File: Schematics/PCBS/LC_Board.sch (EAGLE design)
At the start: 24 parts, among them IC1 ATMEGA328P-AU, Q10 220mA/50V/3.5Ω, U1 LT1763CS8-3.3#TRPBF

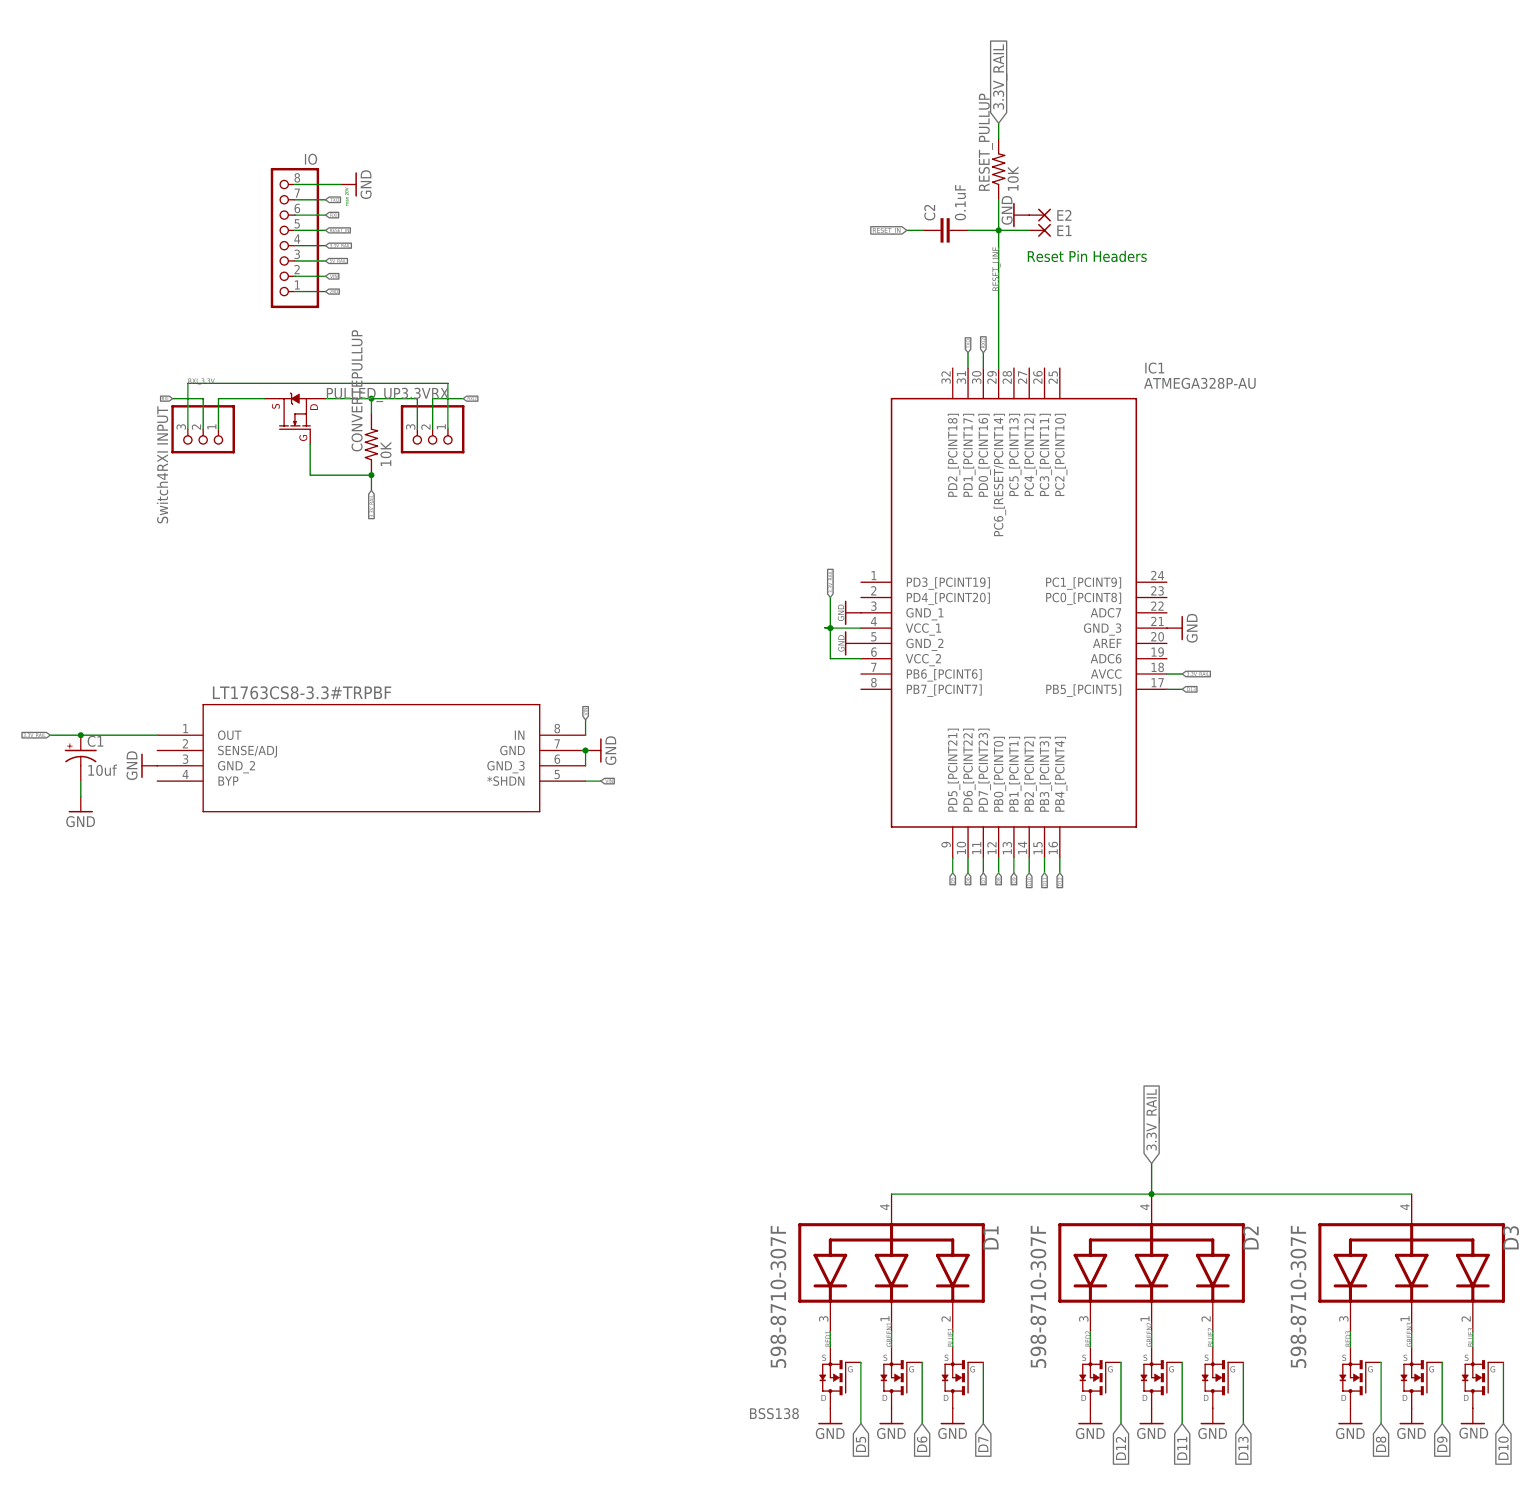
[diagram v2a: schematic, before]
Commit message: updated LC_Board IO to match need pins for Shift registers
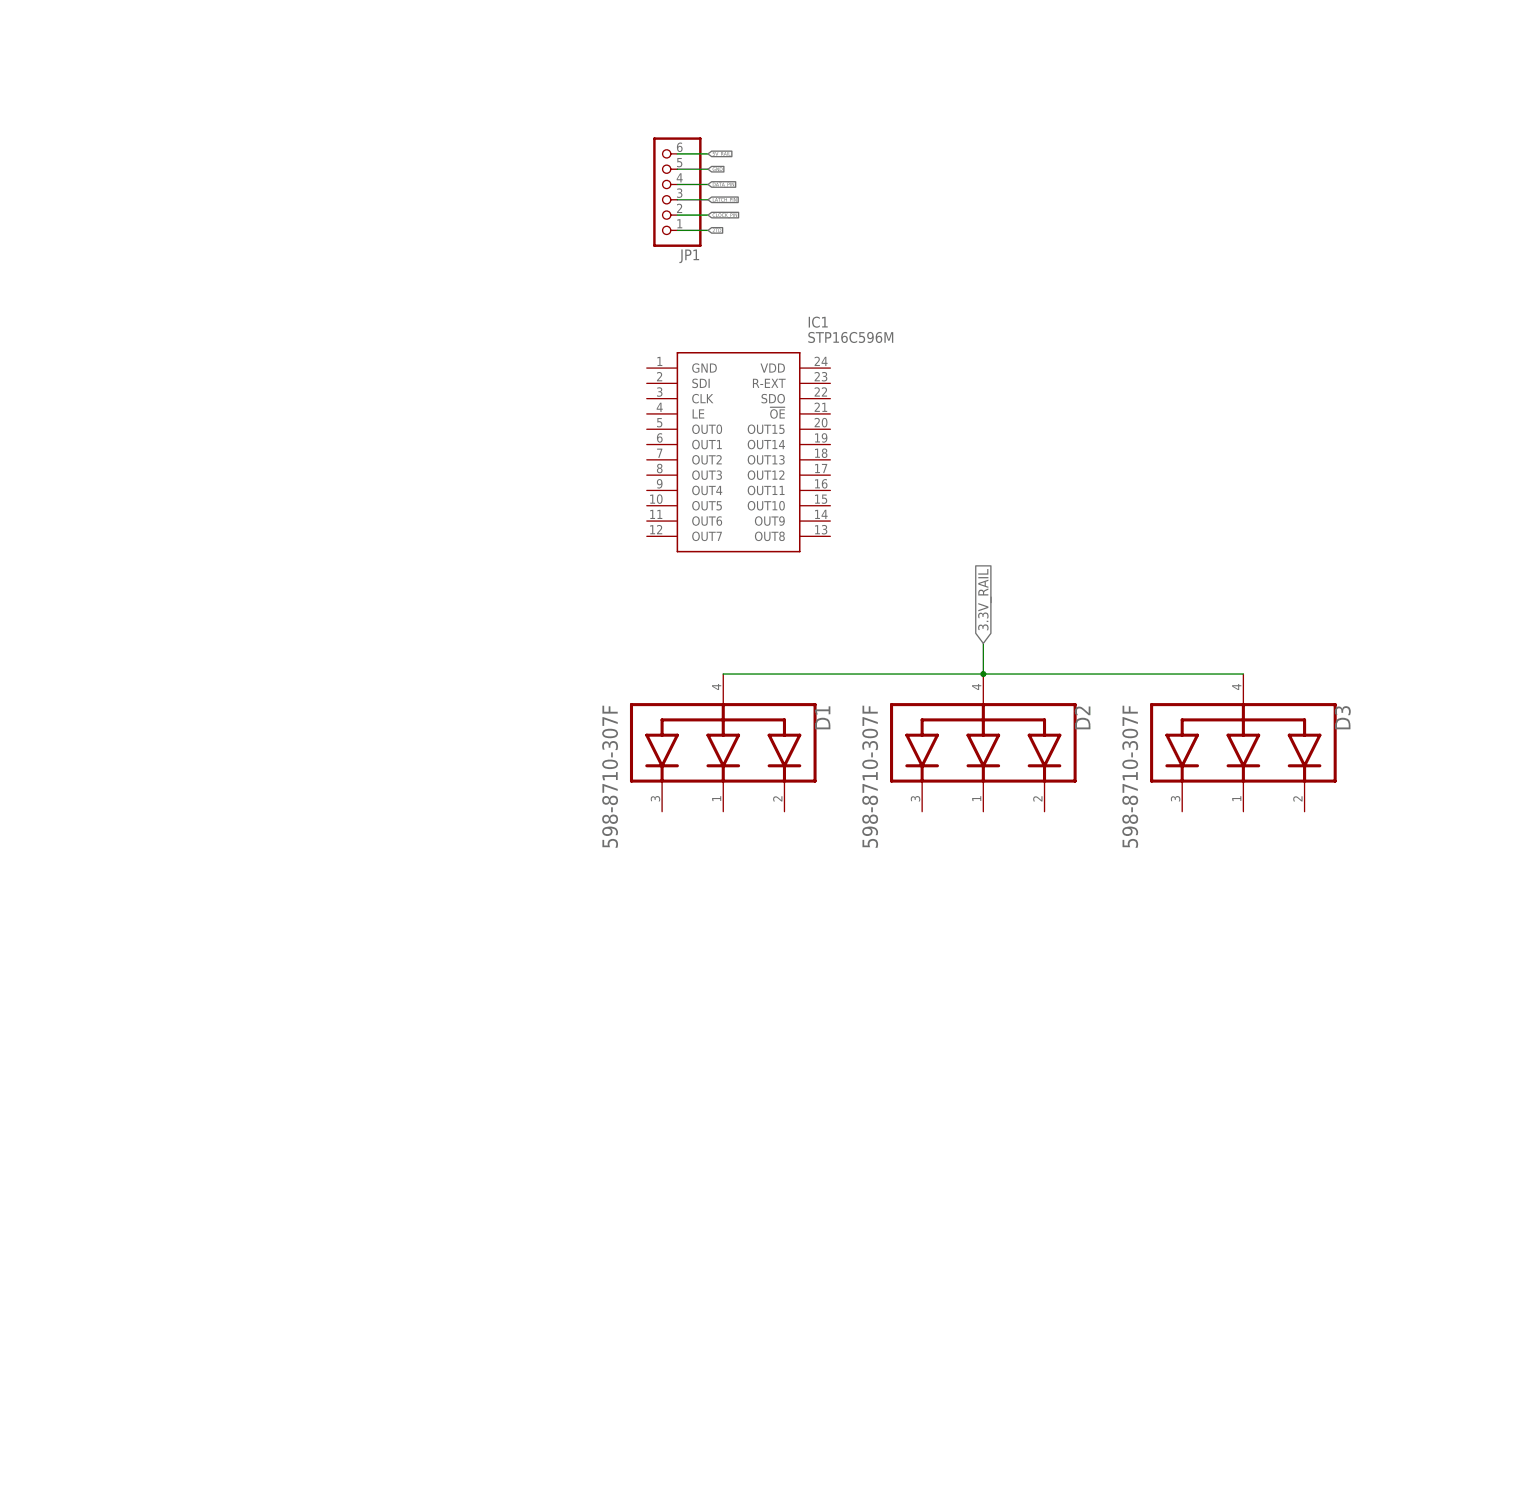
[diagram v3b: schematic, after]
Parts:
- removed C1: 10uf, adafruit:CPOL-USE1.8-4
- removed C2: 0.1uF, SparkFun-Capacitors:0.1UF-0603-25V-(+80/-20%)
- removed CONVERTEPULLUP, RESET_PULLUP: 10K, audio amplifier example:R-US_R0603
- removed E1, E2: DPADS_PAD-0400-S, 52101-101-REV-A:DPADS_PAD-0400-S
- removed JP3: (no value), pinhead:PINHD-1X3
- removed LED1BLUE, LED1GREEN, LED1RED, LED2BLUE, LED2GREEN, LED2RED, LED3BLUE, LED3GREEN, LED3RED: BSS138, 52101-101-REV-A:TRANSISTOR-FET_DMN2004K
- removed Q10: 220mA/50V/3.5Ω, SparkFun-DiscreteSemi:MOSFET-NCH-BSS138
- removed SWITCHINGFROM5VRDITO3.3VRDIINPUT: Switch4RXI INPUT, pinhead:PINHD-1X3
- removed U1: LT1763CS8-3.3#TRPBF, LT1763CS8-3.3_TRPBF:LT1763CS8-3.3#TRPBF
- IC1: value ATMEGA328P-AU -> STP16C596M; device ATMEGA328P-AU:ATMEGA328P-AU -> STP16C596M:STP16C596M; SPICEPREFIX X -> (none)
- JP1: value IO -> (none); device pinhead:PINHD-1X8 -> adafruit:PINHD-1X6CLEAN
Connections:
- net 2BD renamed 2TD
- removed net BLUE1: D1.RED_CATHODE, LED1BLUE.S
- removed net BLUE2: D2.RED_CATHODE, LED2BLUE.S
- removed net BLUE3: D3.RED_CATHODE, LED3BLUE.S
- removed net D10: IC1.PB2_[PCINT2], LED3BLUE.G
- removed net D11: IC1.PB3_[PCINT3], LED2GREEN.G
- removed net D12: IC1.PB4_[PCINT4], LED2RED.G
- removed net D13: IC1.PB5_[PCINT5], LED2BLUE.G
- removed net D5: IC1.PD5_[PCINT21], LED1RED.G
- removed net D6: IC1.PD6_[PCINT22], LED1GREEN.G
- removed net D7: IC1.PD7_[PCINT23], LED1BLUE.G
- removed net D8: IC1.PB0_[PCINT0], LED3RED.G
- removed net D9: IC1.PB1_[PCINT1], LED3GREEN.G
- removed net GREEN1: D1.GREEN_CATHODE, LED1GREEN.S
- removed net GREEN2: D2.GREEN_CATHODE, LED2GREEN.S
- removed net GREEN3: D3.GREEN_CATHODE, LED3GREEN.S
- removed net PULLED_UP3.3VRX: CONVERTEPULLUP.2, JP3.3, Q10.S
- removed net RED1: D1.BLUE_CATHODE, LED1RED.S
- removed net RED2: D2.BLUE_CATHODE, LED2RED.S
- removed net RED3: D3.BLUE_CATHODE, LED3RED.S
- removed net RESET_IN: C2.1, JP1.5
- removed net RESET_LINE: C2.2, E1.P, IC1.PC6_[RESET/PCINT14], RESET_PULLUP.1
- removed net RXD_IN: Q10.D, SWITCHINGFROM5VRDITO3.3VRDIINPUT.1
- removed net RXI: JP1.6, SWITCHINGFROM5VRDITO3.3VRDIINPUT.2
- removed net RXI2: IC1.PD0_[PCINT16], JP3.2
- removed net RXI_3.3V: JP3.1, SWITCHINGFROM5VRDITO3.3VRDIINPUT.3
- removed net TXO: IC1.PD1_[PCINT17], JP1.7
- removed net VIN: JP1.2, U1.*SHDN, U1.IN
- new net CLOCK_PIN: JP1.2
- new net DATA_PIN: JP1.4
- new net LATCH_PIN: JP1.3
- net 3.3V_RAIL: no longer C1.+, CONVERTEPULLUP.1, IC1.AVCC, IC1.VCC_1, IC1.VCC_2, JP1.4, Q10.G, RESET_PULLUP.2, U1.OUT
- net 5V_RAIL: now also JP1.6; no longer JP1.3
- net GND: now also JP1.5; no longer C1.-, E2.P, IC1.GND_1, IC1.GND_2, IC1.GND_3, JP1.8, LED1BLUE.D, LED1GREEN.D, LED1RED.D, LED2BLUE.D, LED2GREEN.D, LED2RED.D, LED3BLUE.D, LED3GREEN.D, LED3RED.D, U1.GND, U1.GND_2, U1.GND_3
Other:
- note removed: "Reset Pin Headers"
- note removed: "max 20V"
- moved on the sheet: D1, D2, D3

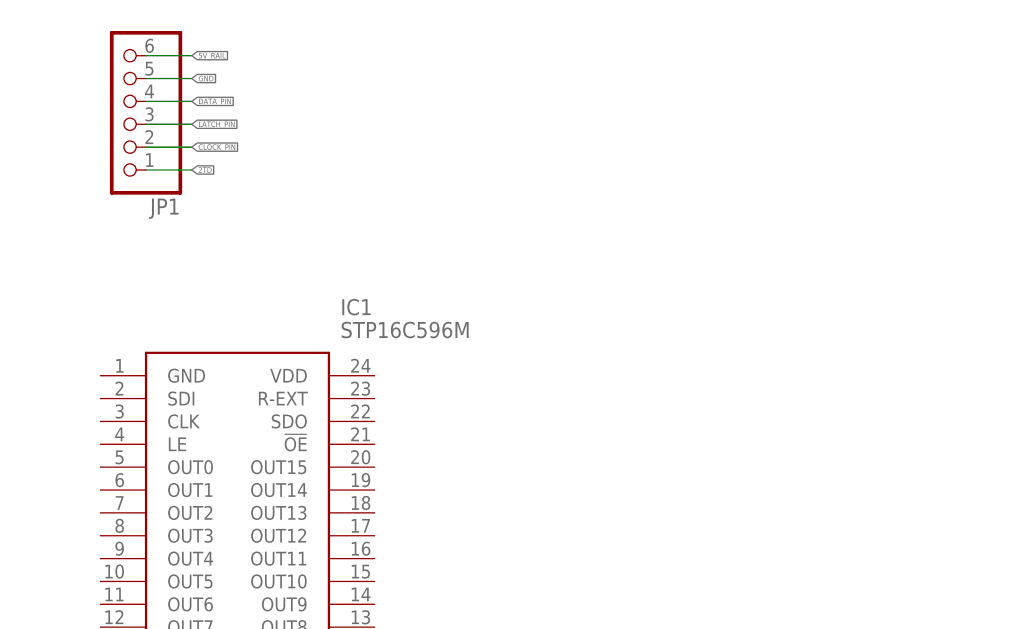
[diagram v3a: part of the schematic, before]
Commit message: added voltage divider and input pins Shift Register
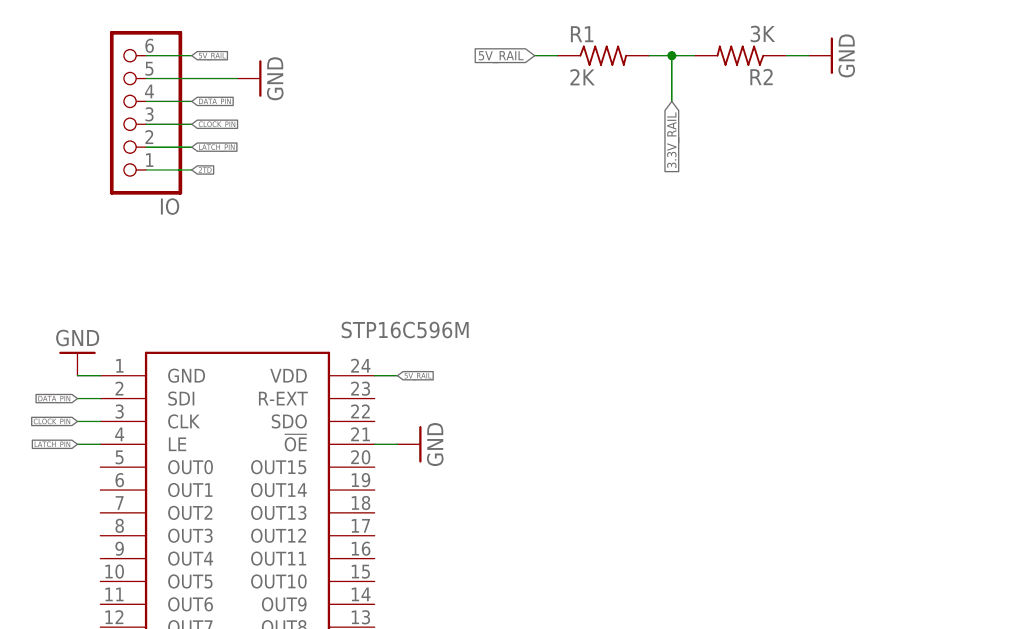
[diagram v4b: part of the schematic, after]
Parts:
- added R1: 2K, adafruit:FLIPFLOP-RES
- added R2: 3K, adafruit:FLIPFLOP-RES
- renumbered JP1 to IO
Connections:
- net 3.3V_RAIL: now also R1.2, R2.2
- net 5V_RAIL: now also IC1.VDD, R1.1
- net CLOCK_PIN: now also IC1.CLK, IO.3; no longer IO.2
- net DATA_PIN: now also IC1.SDI
- net GND: now also IC1.!OE, IC1.GND, R2.1
- net LATCH_PIN: now also IC1.LE, IO.2; no longer IO.3
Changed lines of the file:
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@@
 <?xml version="1.0" encoding="utf-8"?>
 <!DOCTYPE eagle SYSTEM "eagle.dtd">
-<eagle version="9.5.2">
+<eagle version="9.6.2">
 <drawing>
 <settings>
@@
 <part name="FRAME1" library="frames" library_urn="urn:adsk.eagle:library:229" deviceset="A3L-LOC" device=""/>
 <part name="IC1" library="STP16C596M" deviceset="STP16C596M" device=""/>
-<part name="JP1" library="adafruit" library_urn="urn:adsk.eagle:library:420" deviceset="PINHD-1X6" device="CLEAN" package3d_urn="urn:adsk.eagle:package:6240712/1"/>
+<part name="IO" library="adafruit" library_urn="urn:adsk.eagle:library:420" deviceset="PINHD-1X6" device="CLEAN" package3d_urn="urn:adsk.eagle:package:6240712/1"/>
+<part name="R1" library="adafruit" library_urn="urn:adsk.eagle:library:420" deviceset="FLIPFLOP-RES" device="" package3d_urn="urn:adsk.eagle:package:6240726/1" value="2K"/>
+<part name="R2" library="adafruit" library_urn="urn:adsk.eagle:library:420" deviceset="FLIPFLOP-RES" device="" package3d_urn="urn:adsk.eagle:package:6240726/1" value="3K"/>
+<part name="GND1" library="supply1" library_urn="urn:adsk.eagle:library:371" deviceset="GND" device=""/>
+<part name="GND2" library="supply1" library_urn="urn:adsk.eagle:library:371" deviceset="GND" device=""/>
+<part name="GND3" library="supply1" library_urn="urn:adsk.eagle:library:371" deviceset="GND" device=""/>
+<part name="GND4" library="supply1" library_urn="urn:adsk.eagle:library:371" deviceset="GND" device=""/>
 </parts>
 <sheets>
@@
 </instance>
 <instance part="IC1" gate="G$1" x="510.54" y="10.16" smashed="yes">
-<attribute name="NAME" x="537.21" y="17.78" size="1.778" layer="95" align="center-left"/>
 <attribute name="VALUE" x="537.21" y="15.24" size="1.778" layer="96" align="center-left"/>
 </instance>
-<instance part="JP1" gate="A" x="513.08" y="40.64" smashed="yes" rot="R180">
+<instance part="IO" gate="A" x="513.08" y="40.64" smashed="yes" rot="R180">
 <attribute name="NAME" x="519.43" y="29.845" size="1.778" layer="95" rot="R180"/>
 <attribute name="VALUE" x="519.43" y="50.8" size="1.778" layer="96" rot="R180"/>
+</instance>
+<instance part="R1" gate="G$1" x="566.42" y="45.72" smashed="yes">
+<attribute name="NAME" x="562.61" y="47.2186" size="1.778" layer="95"/>
+<attribute name="VALUE" x="562.61" y="42.418" size="1.778" layer="96"/>
+</instance>
+<instance part="R2" gate="G$1" x="581.66" y="45.72" smashed="yes" rot="R180">
+<attribute name="NAME" x="585.47" y="44.2214" size="1.778" layer="95" rot="R180"/>
+<attribute name="VALUE" x="585.47" y="49.022" size="1.778" layer="96" rot="R180"/>
+</instance>
+<instance part="GND1" gate="1" x="528.32" y="43.18" smashed="yes" rot="R90">
+<attribute name="VALUE" x="530.86" y="40.64" size="1.778" layer="96" rot="R90"/>
+</instance>
+<instance part="GND2" gate="1" x="591.82" y="45.72" smashed="yes" rot="R90">
+<attribute name="VALUE" x="594.36" y="43.18" size="1.778" layer="96" rot="R90"/>
+</instance>
+<instance part="GND3" gate="1" x="508" y="12.7" smashed="yes" rot="R180">
+<attribute name="VALUE" x="510.54" y="15.24" size="1.778" layer="96" rot="R180"/>
+</instance>
+<instance part="GND4" gate="1" x="546.1" y="2.54" smashed="yes" rot="R90">
+<attribute name="VALUE" x="548.64" y="0" size="1.778" layer="96" rot="R90"/>
 </instance>
 </instances>
@@
 <label x="566.42" y="-35.56" size="1.6764" layer="95" rot="R90" xref="yes"/>
 </segment>
+<segment>
+<pinref part="R1" gate="G$1" pin="2"/>
+<pinref part="R2" gate="G$1" pin="2"/>
+<wire x1="571.5" y1="45.72" x2="574.04" y2="45.72" width="0.1524" layer="91"/>
+<wire x1="574.04" y1="45.72" x2="576.58" y2="45.72" width="0.1524" layer="91"/>
+<wire x1="574.04" y1="45.72" x2="574.04" y2="40.64" width="0.1524" layer="91"/>
+<junction x="574.04" y="45.72"/>
+<label x="574.04" y="40.64" size="1.016" layer="95" rot="R270" xref="yes"/>
+</segment>
 </net>
 <net name="GND" class="0">
 <segment>
-<pinref part="JP1" gate="A" pin="5"/>
-<wire x1="515.62" y1="43.18" x2="520.7" y2="43.18" width="0.1524" layer="91"/>
-<label x="520.7" y="43.18" size="0.6096" layer="95" xref="yes"/>
+<pinref part="IO" gate="A" pin="5"/>
+<wire x1="515.62" y1="43.18" x2="525.78" y2="43.18" width="0.1524" layer="91"/>
+<pinref part="GND1" gate="1" pin="GND"/>
+</segment>
+<segment>
+<pinref part="R2" gate="G$1" pin="1"/>
+<wire x1="586.74" y1="45.72" x2="589.28" y2="45.72" width="0.1524" layer="91"/>
+<pinref part="GND2" gate="1" pin="GND"/>
+</segment>
+<segment>
+<pinref part="IC1" gate="G$1" pin="GND"/>
+<wire x1="510.54" y1="10.16" x2="508" y2="10.16" width="0.1524" layer="91"/>
+<pinref part="GND3" gate="1" pin="GND"/>
+</segment>
+<segment>
+<pinref part="IC1" gate="G$1" pin="!OE"/>
+<wire x1="541.02" y1="2.54" x2="543.56" y2="2.54" width="0.1524" layer="91"/>
+<pinref part="GND4" gate="1" pin="GND"/>
 </segment>
 </net>
 <net name="5V_RAIL" class="0">
 <segment>
-<pinref part="JP1" gate="A" pin="6"/>
+<pinref part="IO" gate="A" pin="6"/>
 <wire x1="515.62" y1="45.72" x2="520.7" y2="45.72" width="0.1524" layer="91"/>
 <label x="520.7" y="45.72" size="0.6096" layer="95" xref="yes"/>
 </segment>
+<segment>
+<pinref part="R1" gate="G$1" pin="1"/>
+<wire x1="561.34" y1="45.72" x2="558.8" y2="45.72" width="0.1524" layer="91"/>
+<label x="558.8" y="45.72" size="1.016" layer="95" rot="R180" xref="yes"/>
+</segment>
+<segment>
+<pinref part="IC1" gate="G$1" pin="VDD"/>
+<wire x1="541.02" y1="10.16" x2="543.56" y2="10.16" width="0.1524" layer="91"/>
+<label x="543.56" y="10.16" size="0.6096" layer="95" xref="yes"/>
+</segment>
 </net>
 <net name="DATA_PIN" class="0">
 <segment>
-<pinref part="JP1" gate="A" pin="4"/>
+<pinref part="IO" gate="A" pin="4"/>
 <wire x1="515.62" y1="40.64" x2="520.7" y2="40.64" width="0.1524" layer="91"/>
 <label x="520.7" y="40.64" size="0.6096" layer="95" xref="yes"/>
 </segment>
+<segment>
+<pinref part="IC1" gate="G$1" pin="SDI"/>
+<wire x1="510.54" y1="7.62" x2="508" y2="7.62" width="0.1524" layer="91"/>
+<label x="508" y="7.62" size="0.6096" layer="95" rot="R180" xref="yes"/>
+</segment>
 </net>
 <net name="LATCH_PIN" class="0">
 <segment>
-<pinref part="JP1" gate="A" pin="3"/>
+<pinref part="IC1" gate="G$1" pin="LE"/>
+<wire x1="510.54" y1="2.54" x2="508" y2="2.54" width="0.1524" layer="91"/>
+<label x="508" y="2.54" size="0.6096" layer="95" rot="R180" xref="yes"/>
+</segment>
+<segment>
+<pinref part="IO" gate="A" pin="2"/>
+<wire x1="515.62" y1="35.56" x2="520.7" y2="35.56" width="0.1524" layer="91"/>
+<label x="520.7" y="35.56" size="0.6096" layer="95" xref="yes"/>
+</segment>
+</net>
+<net name="CLOCK_PIN" class="0">
+<segment>
+<pinref part="IC1" gate="G$1" pin="CLK"/>
+<wire x1="510.54" y1="5.08" x2="508" y2="5.08" width="0.1524" layer="91"/>
+<label x="508" y="5.08" size="0.6096" layer="95" rot="R180" xref="yes"/>
+</segment>
+<segment>
+<pinref part="IO" gate="A" pin="3"/>
 <wire x1="515.62" y1="38.1" x2="520.7" y2="38.1" width="0.1524" layer="91"/>
 <label x="520.7" y="38.1" size="0.6096" layer="95" xref="yes"/>
 </segment>
 </net>
-<net name="CLOCK_PIN" class="0">
-<segment>
-<pinref part="JP1" gate="A" pin="2"/>
-<wire x1="515.62" y1="35.56" x2="520.7" y2="35.56" width="0.1524" layer="91"/>
-<label x="520.7" y="35.56" size="0.6096" layer="95" xref="yes"/>
-</segment>
-</net>
 <net name="2TD" class="0">
 <segment>
-<pinref part="JP1" gate="A" pin="1"/>
+<pinref part="IO" gate="A" pin="1"/>
 <wire x1="515.62" y1="33.02" x2="520.7" y2="33.02" width="0.1524" layer="91"/>
 <label x="520.7" y="33.02" size="0.6096" layer="95" xref="yes"/>
